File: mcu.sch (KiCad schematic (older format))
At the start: 16 parts, among them SW1 SW_PUSH, U1 STM32F411RE_LQFP64, X1 32.768K, X2 8MHz

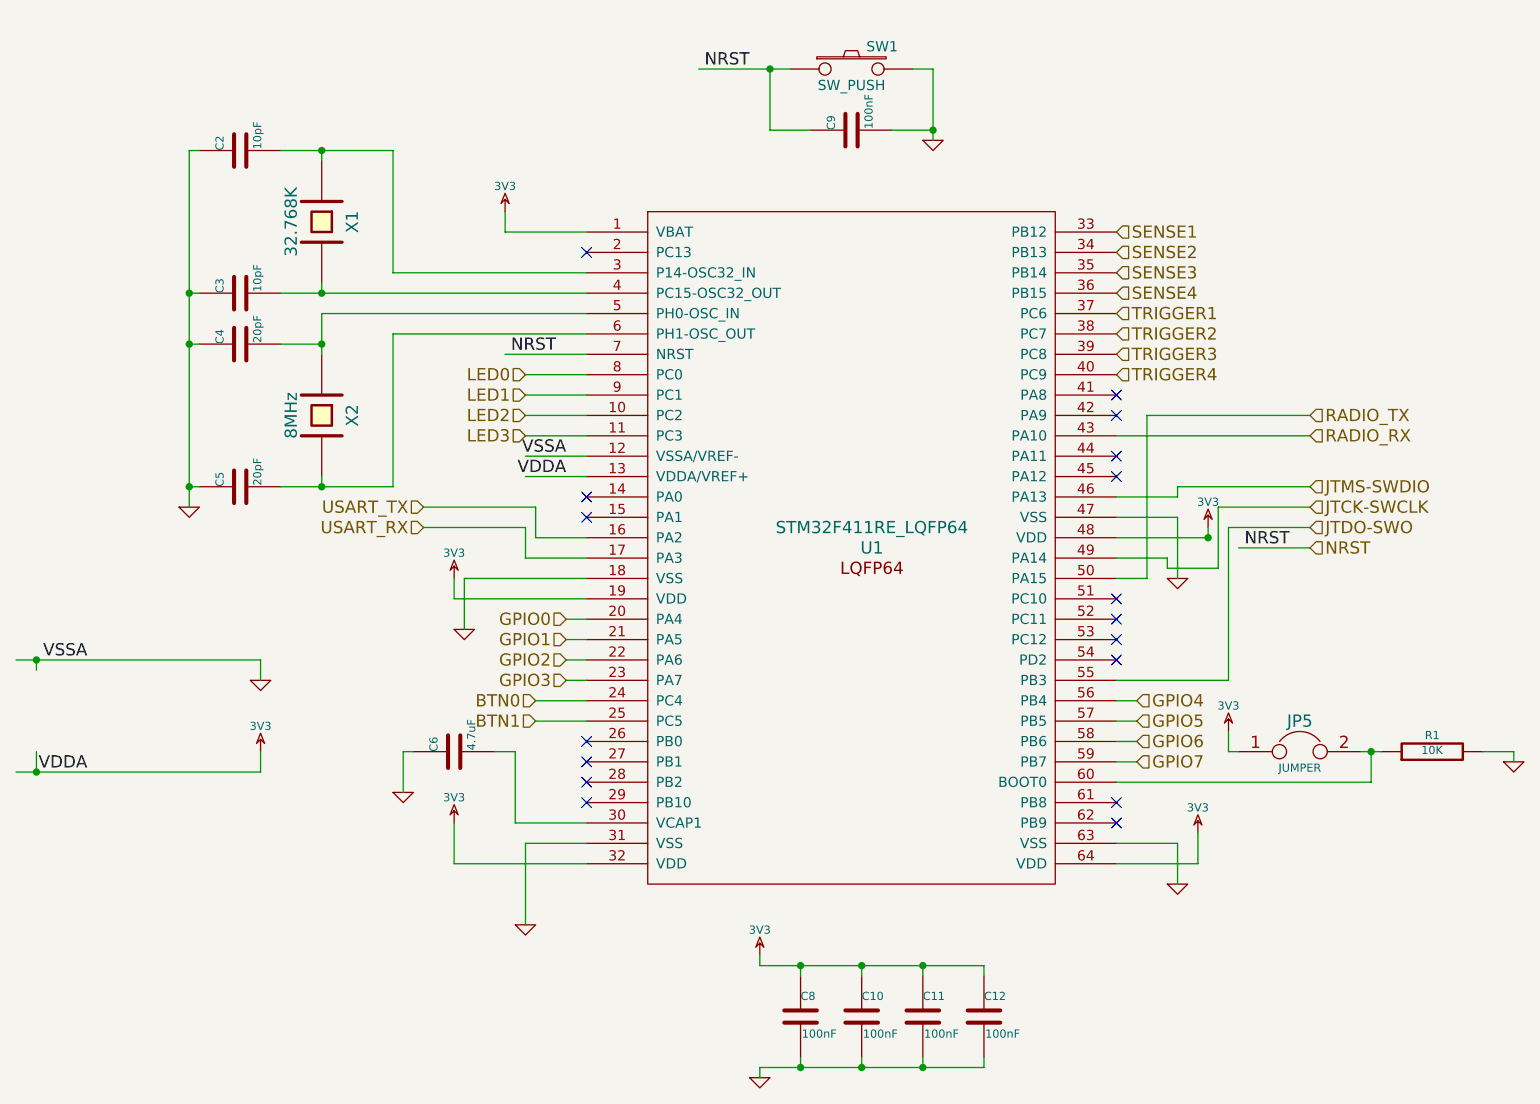
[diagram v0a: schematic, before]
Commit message: Added pyro circuits
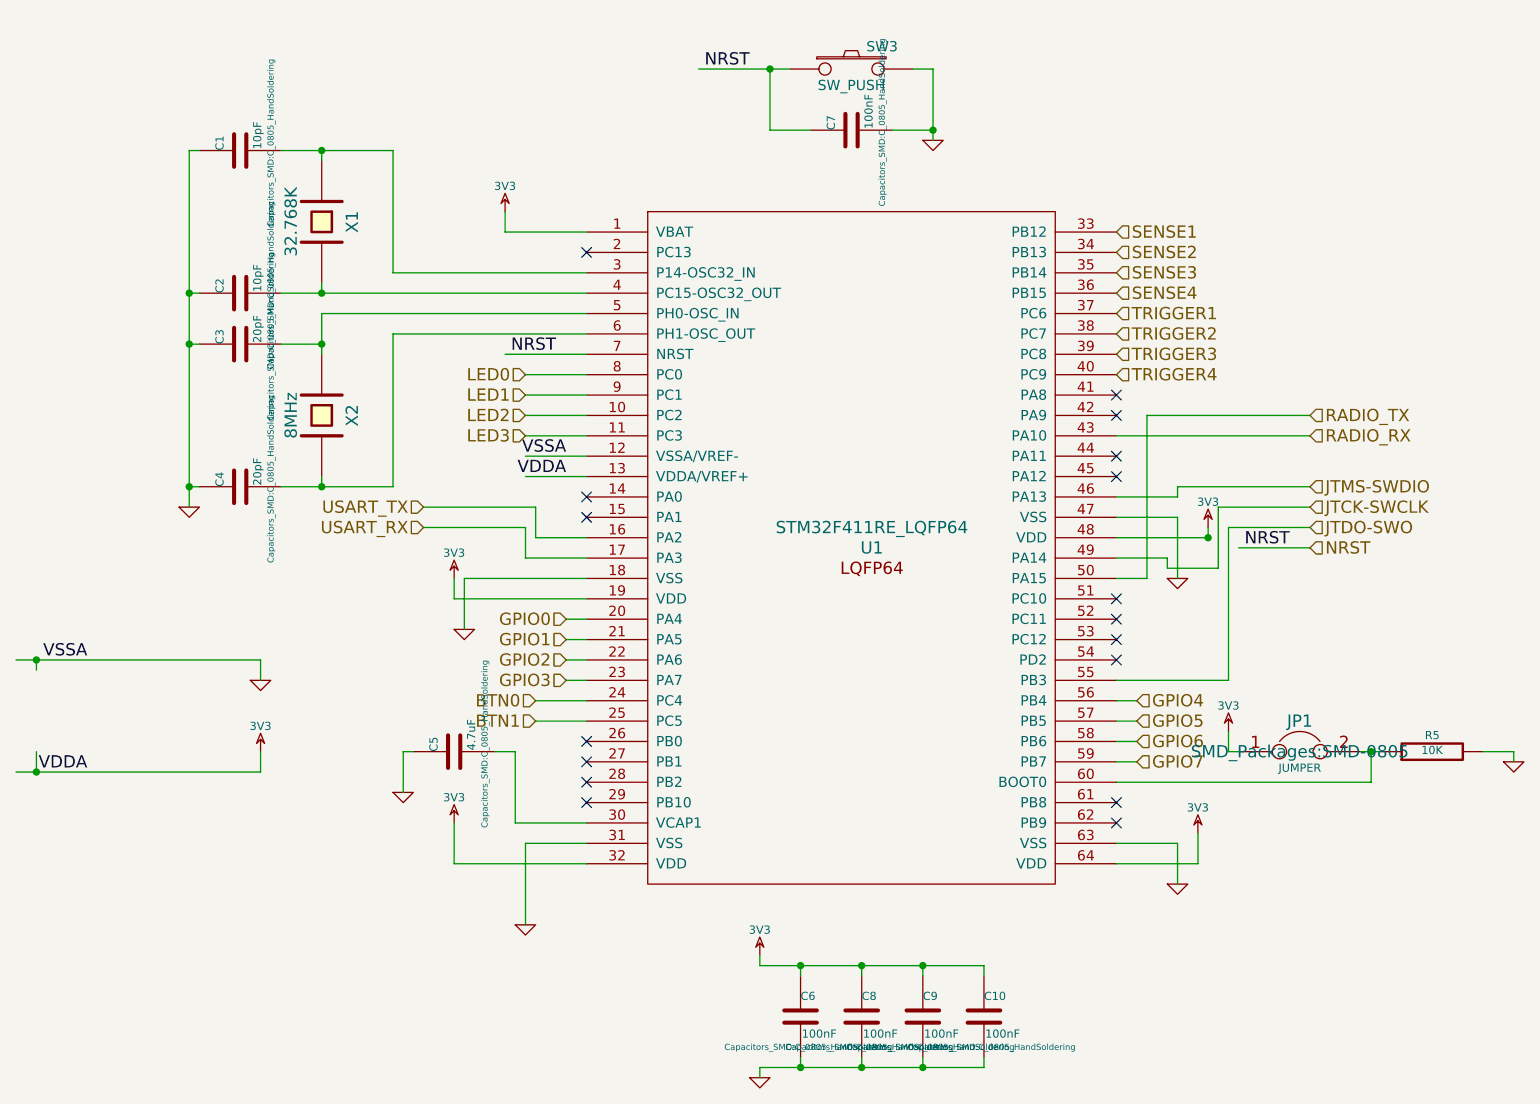
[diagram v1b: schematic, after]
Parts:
- C1: renamed from C2; footprint ~ -> Capacitors_SMD:C_0805_HandSoldering
- C10: renamed from C12; footprint ~ -> Capacitors_SMD:C_0805_HandSoldering
- C2: renamed from C3; footprint ~ -> Capacitors_SMD:C_0805_HandSoldering
- C3: renamed from C4; footprint ~ -> Capacitors_SMD:C_0805_HandSoldering
- C4: renamed from C5; footprint ~ -> Capacitors_SMD:C_0805_HandSoldering
- C5: renamed from C6; footprint ~ -> Capacitors_SMD:C_0805_HandSoldering
- C6: renamed from C8; footprint ~ -> Capacitors_SMD:C_0805_HandSoldering
- C7: renamed from C9; footprint ~ -> Capacitors_SMD:C_0805_HandSoldering
- C8: renamed from C10; footprint ~ -> Capacitors_SMD:C_0805_HandSoldering
- C9: renamed from C11; footprint ~ -> Capacitors_SMD:C_0805_HandSoldering
- JP1: renamed from JP5; footprint ~ -> SMD_Packages:SMD-0805
- R5: renamed from R1; footprint ~ -> Resistors_SMD:R_0805_HandSoldering
- SW3: renamed from SW1; footprint ~ -> (none)
- U1: footprint (none) -> SMD_Packages:VQFP64
- X1, X2: footprint ~ -> (none)
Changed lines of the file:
@@
 LIBS:xbee
 LIBS:avbay-cache
-EELAYER 27 0
+EELAYER 25 0
 EELAYER END
 $Descr USLetter 11000 8500
@@
 F 0 "X1" H 3150 2000 60  0000 C CNN
 F 1 "32.768K" H 3150 1700 60  0000 C CNN
-F 2 "~" H 3150 1850 60  0000 C CNN
+F 2 "" H 3150 1850 60  0001 C CNN
 F 3 "~" H 3150 1850 60  0000 C CNN
 	1    3150 1850
@@
 F 0 "X2" H 3150 2950 60  0000 C CNN
 F 1 "8MHz" H 3150 2650 60  0000 C CNN
-F 2 "~" H 3150 2800 60  0000 C CNN
+F 2 "" H 3150 2800 60  0001 C CNN
 F 3 "~" H 3150 2800 60  0000 C CNN
 	1    3150 2800
@@
 $EndComp
 $Comp
-L C C2
+L C C1
 U 1 1 5430D3C7
 P 2750 1500
-F 0 "C2" H 2750 1600 40  0000 L CNN
+F 0 "C1" H 2750 1600 40  0000 L CNN
 F 1 "10pF" H 2756 1415 40  0000 L CNN
-F 2 "~" H 2788 1350 30  0000 C CNN
+F 2 "Capacitors_SMD:C_0805_HandSoldering" H 2788 1350 30  0000 C CNN
 F 3 "~" H 2750 1500 60  0000 C CNN
 	1    2750 1500
@@
 $EndComp
 $Comp
-L C C3
+L C C2
 U 1 1 5430D401
 P 2750 2200
-F 0 "C3" H 2750 2300 40  0000 L CNN
+F 0 "C2" H 2750 2300 40  0000 L CNN
 F 1 "10pF" H 2756 2115 40  0000 L CNN
-F 2 "~" H 2788 2050 30  0000 C CNN
+F 2 "Capacitors_SMD:C_0805_HandSoldering" H 2788 2050 30  0000 C CNN
 F 3 "~" H 2750 2200 60  0000 C CNN
 	1    2750 2200
@@
 $EndComp
 $Comp
-L C C4
+L C C3
 U 1 1 5430D41B
 P 2750 2450
-F 0 "C4" H 2750 2550 40  0000 L CNN
+F 0 "C3" H 2750 2550 40  0000 L CNN
 F 1 "20pF" H 2756 2365 40  0000 L CNN
-F 2 "~" H 2788 2300 30  0000 C CNN
+F 2 "Capacitors_SMD:C_0805_HandSoldering" H 2788 2300 30  0000 C CNN
 F 3 "~" H 2750 2450 60  0000 C CNN
 	1    2750 2450
@@
 $EndComp
 $Comp
-L C C5
+L C C4
 U 1 1 5430D441
 P 2750 3150
-F 0 "C5" H 2750 3250 40  0000 L CNN
+F 0 "C4" H 2750 3250 40  0000 L CNN
 F 1 "20pF" H 2756 3065 40  0000 L CNN
-F 2 "~" H 2788 3000 30  0000 C CNN
+F 2 "Capacitors_SMD:C_0805_HandSoldering" H 2788 3000 30  0000 C CNN
 F 3 "~" H 2750 3150 60  0000 C CNN
 	1    2750 3150
@@
 NRST
 $Comp
-L SW_PUSH SW1
+L SW_PUSH SW3
 U 1 1 5430D74C
 P 5750 1100
-F 0 "SW1" H 5900 1210 50  0000 C CNN
+F 0 "SW3" H 5900 1210 50  0000 C CNN
 F 1 "SW_PUSH" H 5750 1020 50  0000 C CNN
-F 2 "~" H 5750 1100 60  0000 C CNN
+F 2 "" H 5750 1100 60  0001 C CNN
 F 3 "~" H 5750 1100 60  0000 C CNN
 	1    5750 1100
@@
 $EndComp
 $Comp
-L C C9
+L C C7
 U 1 1 5430D75B
 P 5750 1400
-F 0 "C9" H 5750 1500 40  0000 L CNN
+F 0 "C7" H 5750 1500 40  0000 L CNN
 F 1 "100nF" H 5756 1315 40  0000 L CNN
-F 2 "~" H 5788 1250 30  0000 C CNN
+F 2 "Capacitors_SMD:C_0805_HandSoldering" H 5788 1250 30  0000 C CNN
 F 3 "~" H 5750 1400 60  0000 C CNN
 	1    5750 1400
@@
 $EndComp
 $Comp
-L JUMPER JP5
+L JUMPER JP1
 U 1 1 5430DE18
 P 7950 4450
-F 0 "JP5" H 7950 4600 60  0000 C CNN
+F 0 "JP1" H 7950 4600 60  0000 C CNN
 F 1 "JUMPER" H 7950 4370 40  0000 C CNN
-F 2 "~" H 7950 4450 60  0000 C CNN
+F 2 "SMD_Packages:SMD-0805" H 7950 4450 60  0000 C CNN
 F 3 "~" H 7950 4450 60  0000 C CNN
 	1    7950 4450
@@
 $EndComp
 $Comp
-L R R1
+L R R5
 U 1 1 5430DF6F
 P 8600 4450
-F 0 "R1" V 8680 4450 40  0000 C CNN
+F 0 "R5" V 8680 4450 40  0000 C CNN
 F 1 "10K" V 8607 4451 40  0000 C CNN
-F 2 "~" V 8530 4450 30  0000 C CNN
+F 2 "Resistors_SMD:R_0805_HandSoldering" V 8530 4450 30  0001 C CNN
 F 3 "~" H 8600 4450 30  0000 C CNN
 	1    8600 4450
@@
 $EndComp
 $Comp
-L C C8
+L C C6
 U 1 1 5430E0A1
 P 5500 5750
-F 0 "C8" H 5500 5850 40  0000 L CNN
+F 0 "C6" H 5500 5850 40  0000 L CNN
 F 1 "100nF" H 5506 5665 40  0000 L CNN
-F 2 "~" H 5538 5600 30  0000 C CNN
+F 2 "Capacitors_SMD:C_0805_HandSoldering" H 5538 5600 30  0000 C CNN
 F 3 "~" H 5500 5750 60  0000 C CNN
 	1    5500 5750
@@
 $EndComp
 $Comp
-L C C10
+L C C8
 U 1 1 5430E0BA
 P 5800 5750
-F 0 "C10" H 5800 5850 40  0000 L CNN
+F 0 "C8" H 5800 5850 40  0000 L CNN
 F 1 "100nF" H 5806 5665 40  0000 L CNN
-F 2 "~" H 5838 5600 30  0000 C CNN
+F 2 "Capacitors_SMD:C_0805_HandSoldering" H 5838 5600 30  0000 C CNN
 F 3 "~" H 5800 5750 60  0000 C CNN
 	1    5800 5750
@@
 $EndComp
 $Comp
-L C C11
+L C C9
 U 1 1 5430E0C0
 P 6100 5750
-F 0 "C11" H 6100 5850 40  0000 L CNN
+F 0 "C9" H 6100 5850 40  0000 L CNN
 F 1 "100nF" H 6106 5665 40  0000 L CNN
-F 2 "~" H 6138 5600 30  0000 C CNN
+F 2 "Capacitors_SMD:C_0805_HandSoldering" H 6138 5600 30  0000 C CNN
 F 3 "~" H 6100 5750 60  0000 C CNN
 	1    6100 5750
@@
 $EndComp
 $Comp
-L C C12
+L C C10
 U 1 1 5430E0C6
 P 6400 5750
-F 0 "C12" H 6400 5850 40  0000 L CNN
+F 0 "C10" H 6400 5850 40  0000 L CNN
 F 1 "100nF" H 6406 5665 40  0000 L CNN
-F 2 "~" H 6438 5600 30  0000 C CNN
+F 2 "Capacitors_SMD:C_0805_HandSoldering" H 6438 5600 30  0000 C CNN
 F 3 "~" H 6400 5750 60  0000 C CNN
 	1    6400 5750
@@
 $EndComp
 $Comp
-L C C6
+L C C5
 U 1 1 5430E5B4
 P 3800 4450
-F 0 "C6" H 3800 4550 40  0000 L CNN
+F 0 "C5" H 3800 4550 40  0000 L CNN
 F 1 "4.7uF" H 3806 4365 40  0000 L CNN
-F 2 "~" H 3838 4300 30  0000 C CNN
+F 2 "Capacitors_SMD:C_0805_HandSoldering" H 3838 4300 30  0000 C CNN
 F 3 "~" H 3800 4450 60  0000 C CNN
 	1    3800 4450
@@
 F 0 "U1" H 5850 3450 60  0000 C CNN
 F 1 "STM32F411RE_LQFP64" H 5850 3550 60  0000 C CNN
-F 2 "" H 5850 3600 60  0000 C CNN
+F 2 "SMD_Packages:VQFP64" H 5850 3600 60  0001 C CNN
 F 3 "" H 5850 3600 60  0000 C CNN
 	1    5850 3450

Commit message: Began laying out PCB
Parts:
- SW3: footprint (none) -> Discret:SW_PUSH_SMALL
- U1: footprint SMD_Packages:VQFP64 -> Housings_QFP:TQFP-64_10x10mm_Pitch0.5mm
- X1: footprint (none) -> Crystals:Crystal_HC49-SD_SMD
- X2: footprint (none) -> Crystals:Crystal_HC49-U_Vertical
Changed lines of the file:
@@
 F 0 "X1" H 3150 2000 60  0000 C CNN
 F 1 "32.768K" H 3150 1700 60  0000 C CNN
-F 2 "" H 3150 1850 60  0001 C CNN
+F 2 "Crystals:Crystal_HC49-SD_SMD" H 3150 1850 60  0001 C CNN
 F 3 "~" H 3150 1850 60  0000 C CNN
 	1    3150 1850
@@
 F 0 "X2" H 3150 2950 60  0000 C CNN
 F 1 "8MHz" H 3150 2650 60  0000 C CNN
-F 2 "" H 3150 2800 60  0001 C CNN
+F 2 "Crystals:Crystal_HC49-U_Vertical" H 3150 2800 60  0001 C CNN
 F 3 "~" H 3150 2800 60  0000 C CNN
 	1    3150 2800
@@
 F 0 "SW3" H 5900 1210 50  0000 C CNN
 F 1 "SW_PUSH" H 5750 1020 50  0000 C CNN
-F 2 "" H 5750 1100 60  0001 C CNN
+F 2 "Discret:SW_PUSH_SMALL" H 5750 1100 60  0001 C CNN
 F 3 "~" H 5750 1100 60  0000 C CNN
 	1    5750 1100
@@
 F 0 "U1" H 5850 3450 60  0000 C CNN
 F 1 "STM32F411RE_LQFP64" H 5850 3550 60  0000 C CNN
-F 2 "SMD_Packages:VQFP64" H 5850 3600 60  0001 C CNN
+F 2 "Housings_QFP:TQFP-64_10x10mm_Pitch0.5mm" H 5850 3600 60  0001 C CNN
 F 3 "" H 5850 3600 60  0000 C CNN
 	1    5850 3450
